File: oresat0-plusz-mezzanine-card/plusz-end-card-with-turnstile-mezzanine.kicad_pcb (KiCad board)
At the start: 8 copper layers, 80 x 71.5 mm, 22 parts, among them J1 Conn_Coaxial, U1 QBA-07+, U2 QBA-07+, U3 QBA-07+

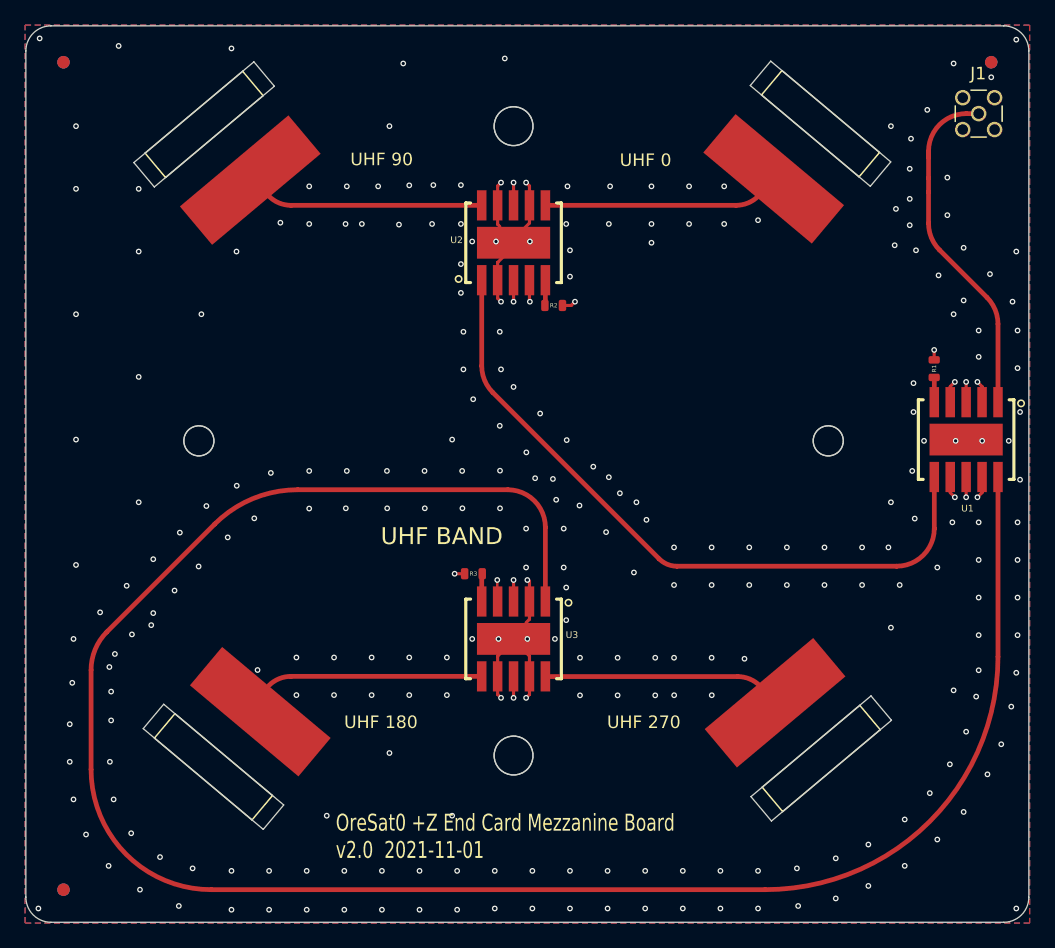
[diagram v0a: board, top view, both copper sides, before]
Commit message: Design Corrections for Ordering
- Adjusted solder mask clearance
- Changed trace width for JLC stackup

Co-Authored-By: Valles1 <134664903+Valles1@users.noreply.github.com>
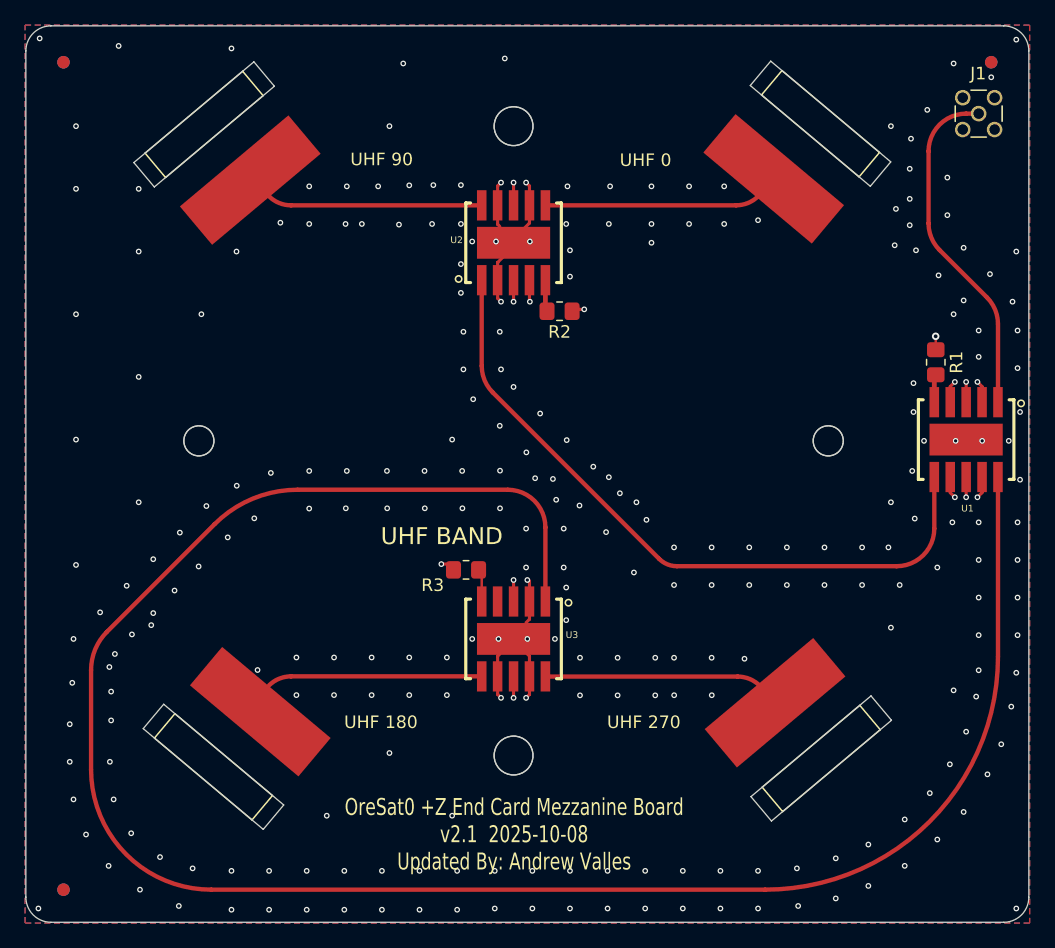
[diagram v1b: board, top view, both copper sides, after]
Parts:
- added G***: LOGO, LOGO, B.Cu at (150.9, 102.8)
- R1, R2, R3: footprint plusz-end-card-with-turnstile-mezzanine:.0603-C-NOSILK -> Resistor_SMD:R_0805_2012Metric_Pad1.20x1.40mm_HandSolder
- moved R3 0.67 mm to (144.7, 111.0)
- moved R2 0.66 mm to (152.2, 90.4)
- moved R1 0.52 mm to (182.2, 94.4)
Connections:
- net UHF renamed /plusz-end-card-with-turnstile-mezzanine_1/UHF
- net UHF-SHORT renamed /plusz-end-card-with-turnstile-mezzanine_1/UHF-SHORT
- net UHF-SHORT+1/4WAVE renamed /plusz-end-card-with-turnstile-mezzanine_1/UHF-SHORT+1/4WAVE
- FIDUCIAL1 pad FIDUCIAL: (no net) -> unconnected-(FIDUCIAL1-PadFIDUCIAL)
- FIDUCIAL2 pad FIDUCIAL: (no net) -> unconnected-(FIDUCIAL2-PadFIDUCIAL)
- FIDUCIAL3 pad FIDUCIAL: (no net) -> unconnected-(FIDUCIAL3-PadFIDUCIAL)
- FIDUCIAL4 pad FIDUCIAL: (no net) -> unconnected-(FIDUCIAL4-PadFIDUCIAL)
- FIDUCIAL6 pad FIDUCIAL: (no net) -> unconnected-(FIDUCIAL6-PadFIDUCIAL)
- FIDUCIAL7 pad FIDUCIAL: (no net) -> unconnected-(FIDUCIAL7-PadFIDUCIAL)
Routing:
- net GND: track 47.4 -> 46.0 mm, vias 284 -> 283
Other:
- copper layers 8 -> 4
- board text added: "OreSat0 +Z End Card Mezzanine Board v2.1 2025-10-08 Updated By: Andrew Valles"
- board text removed: "${REFERENCE}"
- board text removed: "L1 BAND"
- board text removed: "OreSat0 +Z End Card Mezzanine Board v2.0 2021-11-01"
